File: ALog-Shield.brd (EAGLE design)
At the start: 53.3 x 78.5 mm, 28 parts, among them U1 DS3231MZ/V+T

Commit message: DRC: routing
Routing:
- net +3V3: track 186.7 -> 123.0 mm, vias 0 -> 1
- net RESET: track 0.00 -> 41.9 mm
- net N$11: track 0.00 -> 24.5 mm
- net GND: vias 2 -> 3
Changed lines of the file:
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@@
 <?xml version="1.0" encoding="utf-8"?>
 <!DOCTYPE eagle SYSTEM "eagle.dtd">
-<eagle version="8.3.1">
+<eagle version="8.5.0">
 <drawing>
 <settings>
@@
 <param name="dpMaxLengthDifference" value="10mm"/>
 <param name="dpGapFactor" value="2.5"/>
-<param name="checkGrid" value="0"/>
 <param name="checkAngle" value="0"/>
 <param name="checkFont" value="1"/>
 <param name="checkRestrict" value="1"/>
+<param name="checkStop" value="0"/>
+<param name="checkValues" value="0"/>
 <param name="useDiameter" value="13"/>
 <param name="maxErrors" value="50"/>
@@
 <wire x1="9.5504" y1="29.2608" x2="9.6140125" y2="29.2418" width="0.2032" layer="1"/>
 <contactref element="CLK_DECOUP" pad="2"/>
+<via x="33.782" y="48.26" extent="1-16" drill="0.3048" shape="octagon"/>
 </signal>
 <signal name="VCC">
@@
 <contactref element="H4" pad="2"/>
 <wire x1="8.7376" y1="66.8528" x2="8.7376" y2="74.5744" width="0.2032" layer="1"/>
-<wire x1="13.6144" y1="61.976" x2="8.7376" y2="66.8528" width="0.2032" layer="1"/>
+<wire x1="13.6144" y1="61.976" x2="10.7442" y2="64.8462" width="0.2032" layer="1"/>
+<wire x1="10.7442" y1="64.8462" x2="8.7376" y2="66.8528" width="0.2032" layer="1"/>
 <wire x1="8.7376" y1="74.5744" x2="8.58" y2="74.676" width="0.2032" layer="1"/>
 <wire x1="13.6144" y1="61.976" x2="13.6525" y2="61.976" width="0.2032" layer="1"/>
@@
 <contactref element="U$9" pad="RES"/>
 <contactref element="RESET" pad="2"/>
-<wire x1="17.4625" y1="13.716" x2="47.622" y2="6.647" width="0" layer="19" extent="1-1"/>
+<wire x1="47.6504" y1="11.7348" x2="47.6504" y2="6.7564" width="0.2032" layer="1"/>
+<wire x1="49.2506" y1="13.335" x2="47.6504" y2="11.7348" width="0.2032" layer="1"/>
+<wire x1="49.2506" y1="14.224" x2="49.2506" y2="13.335" width="0.2032" layer="1"/>
+<wire x1="48.5394" y1="14.9352" x2="49.2506" y2="14.224" width="0.2032" layer="1"/>
+<wire x1="33.0708" y1="14.9352" x2="48.5394" y2="14.9352" width="0.2032" layer="1"/>
+<wire x1="30.5816" y1="12.446" x2="33.0708" y2="14.9352" width="0.2032" layer="1"/>
+<wire x1="18.8468" y1="12.446" x2="30.5816" y2="12.446" width="0.2032" layer="1"/>
+<wire x1="17.6022" y1="13.6906" x2="18.8468" y2="12.446" width="0.2032" layer="1"/>
+<wire x1="47.6504" y1="6.7564" x2="47.622" y2="6.647" width="0.2032" layer="1"/>
+<wire x1="17.6022" y1="13.6906" x2="17.4625" y2="13.716" width="0.2032" layer="1"/>
 </signal>
 <signal name="A2">
@@
 <wire x1="20.1168" y1="6.2992" x2="19.5072" y2="6.2992" width="0.2032" layer="16"/>
 <wire x1="15.6464" y1="3.8608" x2="15.58" y2="3.81" width="0.2032" layer="16"/>
-<wire x1="19.9136" y1="20.5232" x2="19.9136" y2="13.8176" width="0.2032" layer="16"/>
-<wire x1="6.5024" y1="33.9344" x2="19.9136" y2="20.5232" width="0.2032" layer="16"/>
-<wire x1="6.5024" y1="57.0992" x2="6.5024" y2="37.5158" width="0.2032" layer="16"/>
-<wire x1="6.5024" y1="37.5158" x2="6.5024" y2="33.9344" width="0.2032" layer="16"/>
-<wire x1="2.2352" y1="61.3664" x2="6.5024" y2="57.0992" width="0.2032" layer="16"/>
-<wire x1="2.2352" y1="62.5856" x2="2.2352" y2="61.3664" width="0.2032" layer="16"/>
-<wire x1="3.4544" y1="63.8048" x2="2.2352" y2="62.5856" width="0.2032" layer="16"/>
-<wire x1="6.7056" y1="63.8048" x2="3.4544" y2="63.8048" width="0.2032" layer="16"/>
-<wire x1="8.5344" y1="61.976" x2="7.6073" y2="62.9031" width="0.2032" layer="16"/>
-<wire x1="7.6073" y1="62.9031" x2="6.7056" y2="63.8048" width="0.2032" layer="16"/>
-<wire x1="19.9136" y1="13.8176" x2="20.0025" y2="13.716" width="0.2032" layer="16"/>
-<wire x1="28.0416" y1="74.7776" x2="29.464" y2="74.7776" width="0.2032" layer="16"/>
-<wire x1="26.8224" y1="75.9968" x2="28.0416" y2="74.7776" width="0.2032" layer="16"/>
-<wire x1="21.9456" y1="75.9968" x2="26.8224" y2="75.9968" width="0.2032" layer="16"/>
-<wire x1="20.5232" y1="74.5744" x2="21.9456" y2="75.9968" width="0.2032" layer="16"/>
-<wire x1="20.5232" y1="73.7616" x2="20.5232" y2="74.5744" width="0.2032" layer="16"/>
-<wire x1="8.7376" y1="61.976" x2="9.652" y2="62.8904" width="0.2032" layer="16"/>
-<wire x1="9.652" y1="62.8904" x2="20.5232" y2="73.7616" width="0.2032" layer="16"/>
-<wire x1="29.464" y1="74.7776" x2="29.58" y2="74.676" width="0.2032" layer="16"/>
 <contactref element="LSHIFT1" pad="1"/>
 <contactref element="SD1" pad="4"/>
@@
 <wire x1="29.6926" y1="74.676" x2="29.58" y2="74.676" width="0.2032" layer="1"/>
 <contactref element="JP1" pad="2"/>
-<wire x1="6.5024" y1="37.5158" x2="15.113" y2="37.5158" width="0.2032" layer="16"/>
-<wire x1="15.113" y1="37.5158" x2="15.24" y2="37.4142" width="0.2032" layer="16"/>
-<wire x1="8.001" y1="63.2968" x2="7.6073" y2="62.9031" width="0.2032" layer="16"/>
-<wire x1="9.2456" y1="63.2968" x2="8.001" y2="63.2968" width="0.2032" layer="16"/>
-<wire x1="9.652" y1="62.8904" x2="9.2456" y2="63.2968" width="0.2032" layer="16"/>
+<wire x1="15.113" y1="35.0266" x2="15.113" y2="37.338" width="0.2032" layer="16"/>
+<wire x1="14.5796" y1="34.4932" x2="15.113" y2="35.0266" width="0.2032" layer="16"/>
+<wire x1="14.5796" y1="19.2024" x2="14.5796" y2="33.0708" width="0.2032" layer="16"/>
+<wire x1="14.5796" y1="33.0708" x2="14.5796" y2="34.4932" width="0.2032" layer="16"/>
+<wire x1="19.9136" y1="13.8684" x2="14.5796" y2="19.2024" width="0.2032" layer="16"/>
+<wire x1="15.113" y1="37.338" x2="15.24" y2="37.4142" width="0.2032" layer="16"/>
+<wire x1="19.9136" y1="13.8684" x2="20.0025" y2="13.716" width="0.2032" layer="16"/>
+<wire x1="24.5364" y1="33.0708" x2="14.5796" y2="33.0708" width="0.2032" layer="16"/>
+<wire x1="26.67" y1="33.0708" x2="24.5364" y2="33.0708" width="0.2032" layer="1"/>
+<wire x1="27.0256" y1="33.4264" x2="26.67" y2="33.0708" width="0.2032" layer="1"/>
+<wire x1="27.0256" y1="33.4264" x2="27.04" y2="33.563" width="0.2032" layer="1"/>
+<via x="24.5364" y="33.0708" extent="1-16" drill="0.3302"/>
 </signal>
 <signal name="SCL">
@@
 <wire x1="8.128" y1="56.2864" x2="14.4272" y2="49.9872" width="0.2032" layer="1"/>
 <wire x1="8.128" y1="59.5376" x2="8.128" y2="56.2864" width="0.2032" layer="1"/>
-<wire x1="6.096" y1="61.5696" x2="8.128" y2="59.5376" width="0.2032" layer="1"/>
+<wire x1="6.096" y1="61.5696" x2="6.4008" y2="61.2648" width="0.2032" layer="1"/>
+<wire x1="6.4008" y1="61.2648" x2="8.128" y2="59.5376" width="0.2032" layer="1"/>
 <wire x1="6.096" y1="61.976" x2="6.096" y2="61.5696" width="0.2032" layer="1"/>
 <wire x1="16.0528" y1="51.2064" x2="16.129" y2="51.3588" width="0.2032" layer="1"/>
@@
 <contactref element="LOG" pad="2"/>
 <contactref element="D2" pad="3"/>
-<wire x1="44.958" y1="49.7" x2="50.422" y2="71.585" width="0" layer="19" extent="1-1"/>
+<wire x1="50.3174" y1="54.5846" x2="50.3174" y2="71.4756" width="0.2032" layer="1"/>
+<wire x1="45.5168" y1="49.784" x2="50.3174" y2="54.5846" width="0.2032" layer="1"/>
+<wire x1="44.9834" y1="49.784" x2="45.5168" y2="49.784" width="0.2032" layer="1"/>
+<wire x1="50.3174" y1="71.4756" x2="50.422" y2="71.585" width="0.2032" layer="1"/>
+<wire x1="44.9834" y1="49.784" x2="44.958" y2="49.7" width="0.2032" layer="1"/>
 </signal>
 <signal name="D4">

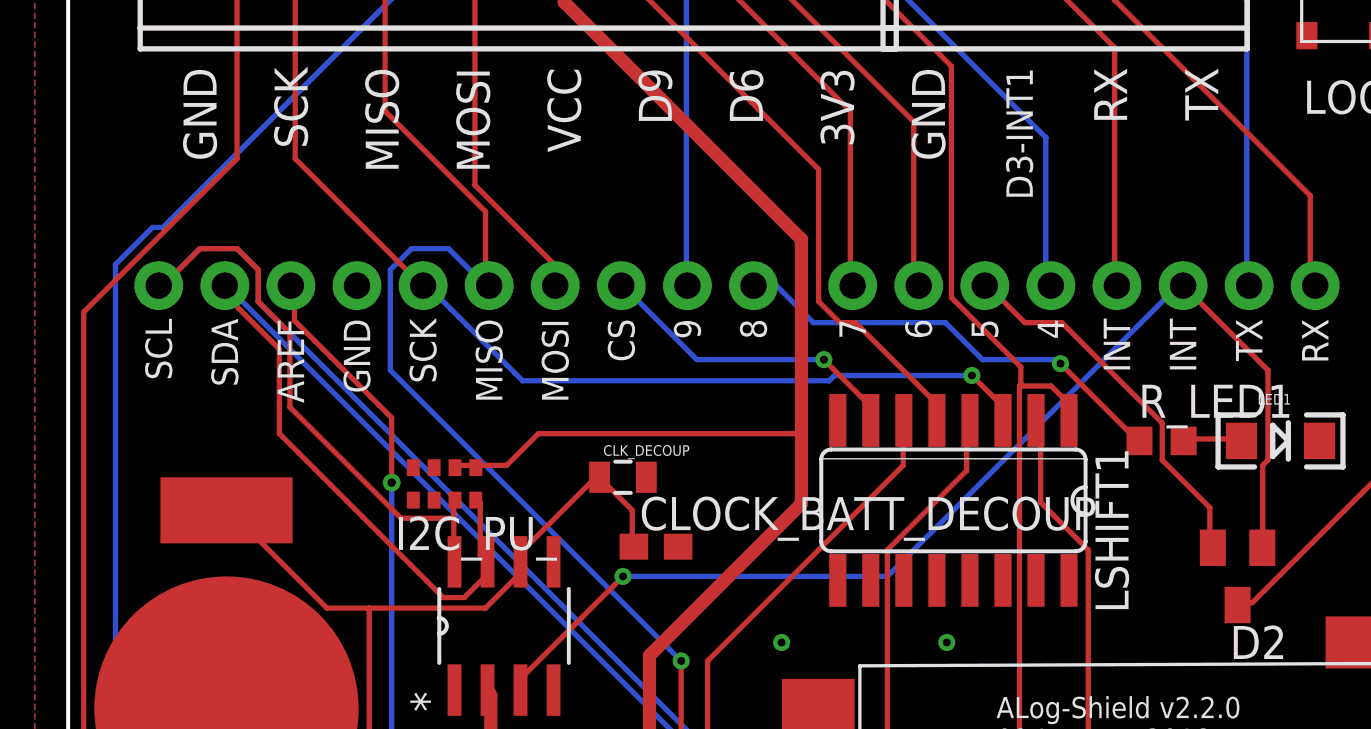
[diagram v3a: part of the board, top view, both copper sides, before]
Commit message: 3.3K RTC PU array to discrete (10K?)
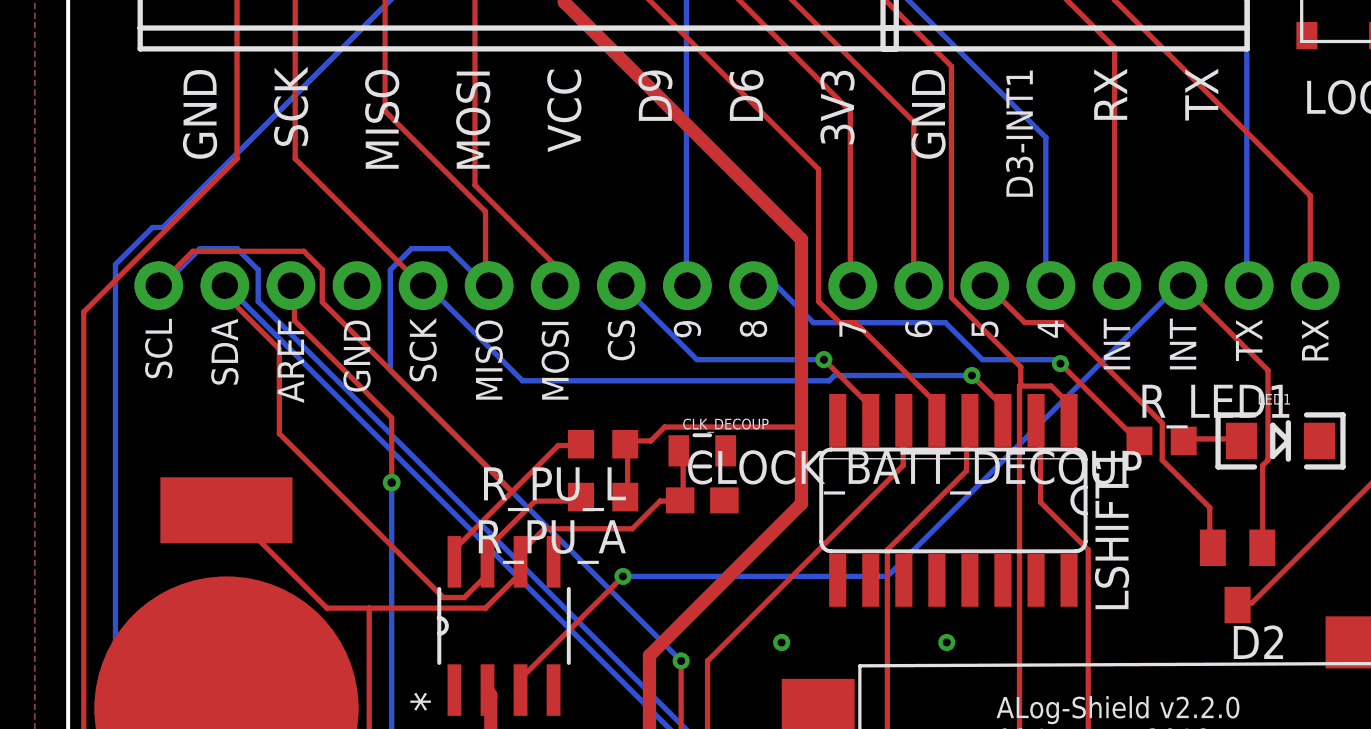
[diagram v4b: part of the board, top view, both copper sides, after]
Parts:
- removed I2C_PU_: 3.3K, resistor-dil:0603-ARC
- added R_PU_A, R_PU_L: 10k, resistor:R0603
- moved CLK_DECOUP 3.21 mm to (24.4, 55.6)
- moved CLOCK_BATT_DECOUP 2.51 mm to (24.4, 53.7)
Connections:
- net SCL: now also R_PU_L.2; no longer I2C_PU_.3
- net SDA: now also R_PU_A.2; no longer I2C_PU_.4
- net VCC: now also R_PU_A.1, R_PU_L.1; no longer I2C_PU_.5, I2C_PU_.6
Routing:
- net SCL: track 103.2 -> 108.0 mm
- net VCC: track 112.2 -> 107.5 mm
- net SDA: track 97.5 -> 99.9 mm
- net BAT: track 35.6 -> 37.2 mm
